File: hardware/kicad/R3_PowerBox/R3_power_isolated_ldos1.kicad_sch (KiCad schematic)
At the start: 12 parts, among them U4 ADM7150ACPZ-3.3-R7, U5 TPS7A2033PDBVR

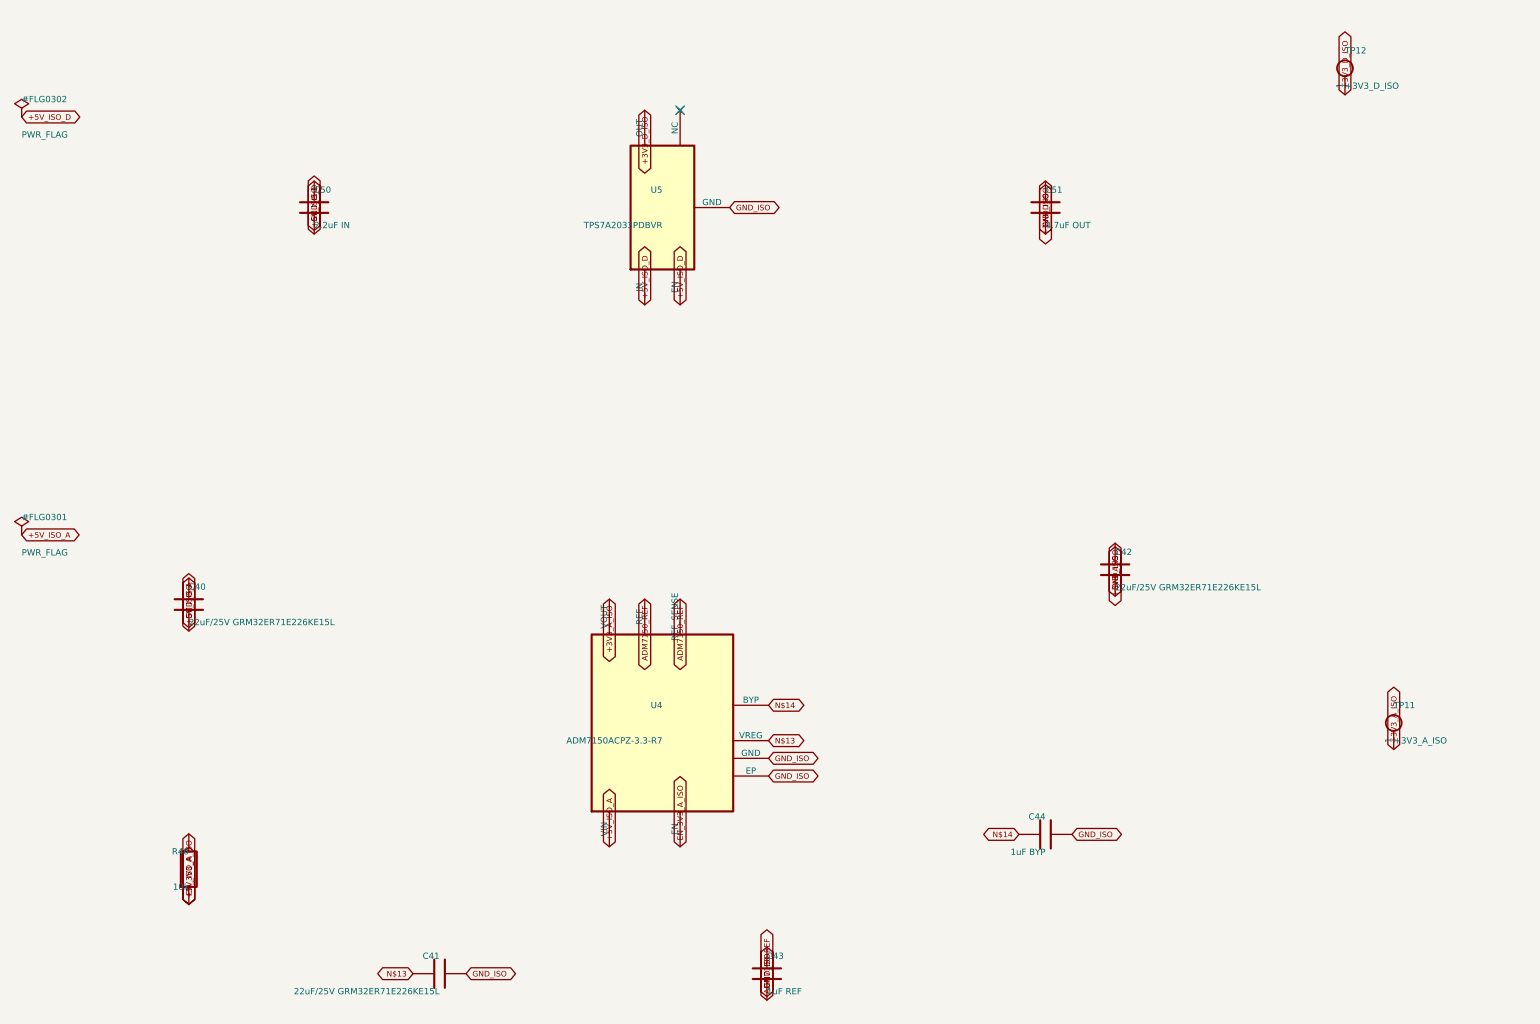
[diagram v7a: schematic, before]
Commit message: Rev.A review fixes: final CAD verification and documented hardware gates
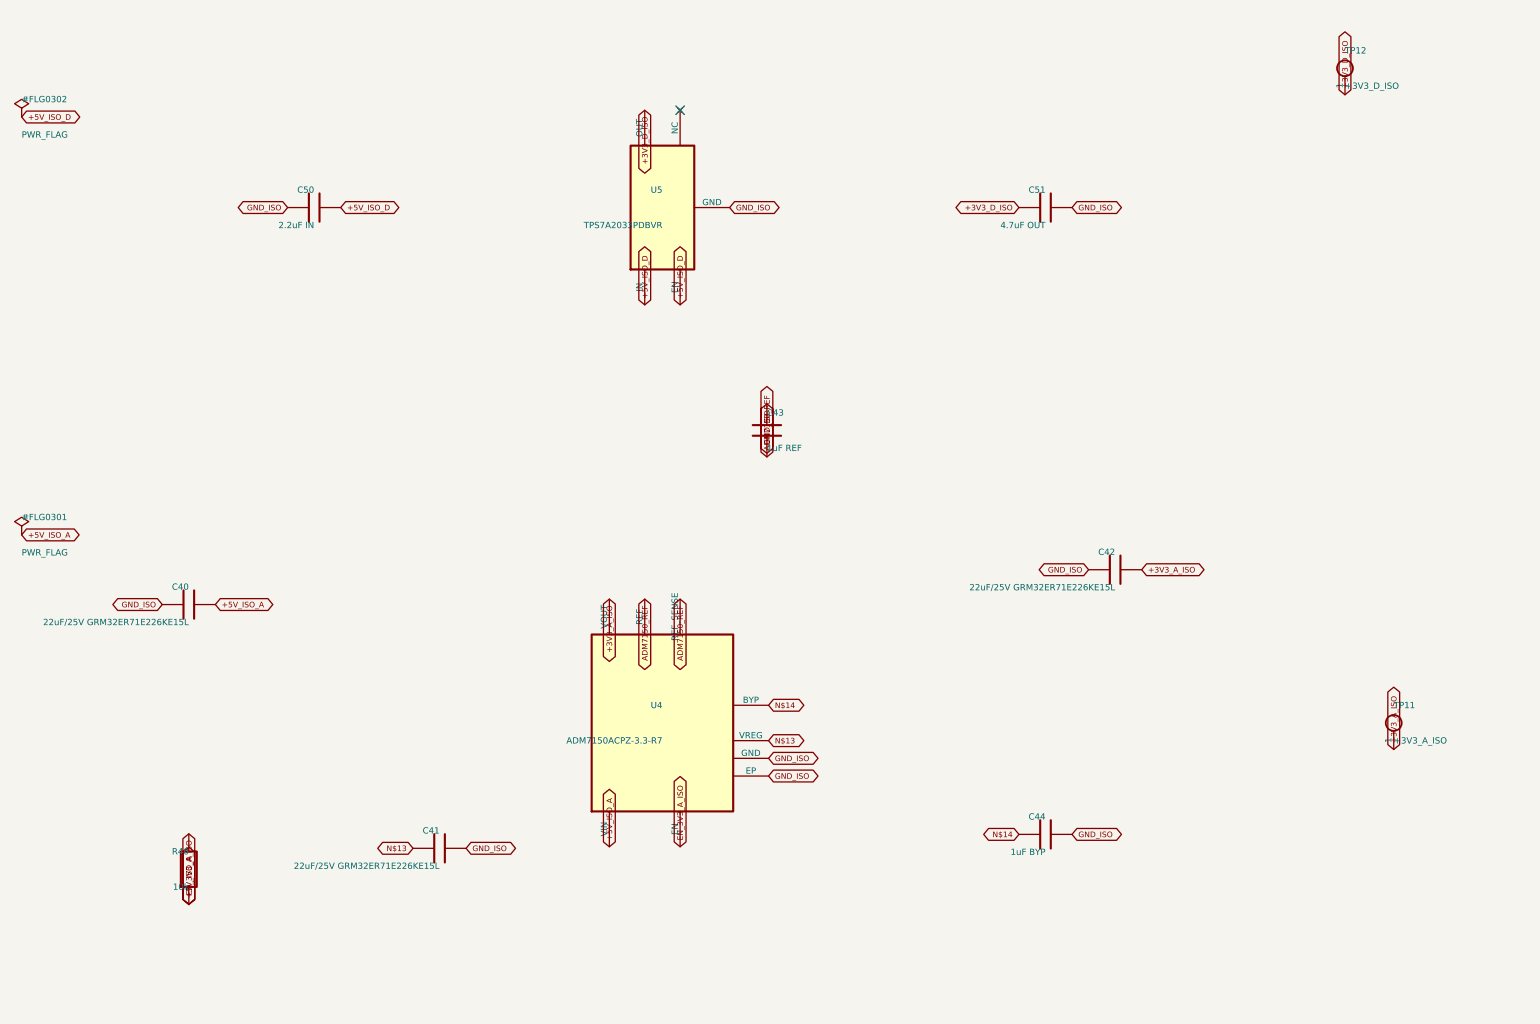
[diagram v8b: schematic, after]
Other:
- moved on the sheet: C40, C41, C42, C43, C50, C51
